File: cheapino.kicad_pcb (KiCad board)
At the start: 2 copper layers, 130.3 x 94.5 mm, 42 parts, among them K1 SW_Push, K10 SW_Push, K11 SW_Push, K12 SW_Push, K13 SW_Push, K14 SW_Push, K15 SW_Push, K16 SW_Push, K17 SW_Push, K18 SW_Push, K2 SW_Push, K3 SW_Push, K4 SW_Push, K5 SW_Push, K6 SW_Push, K7 SW_Push, K8 SW_Push, K9 SW_Push, U1 RP2040-Zero

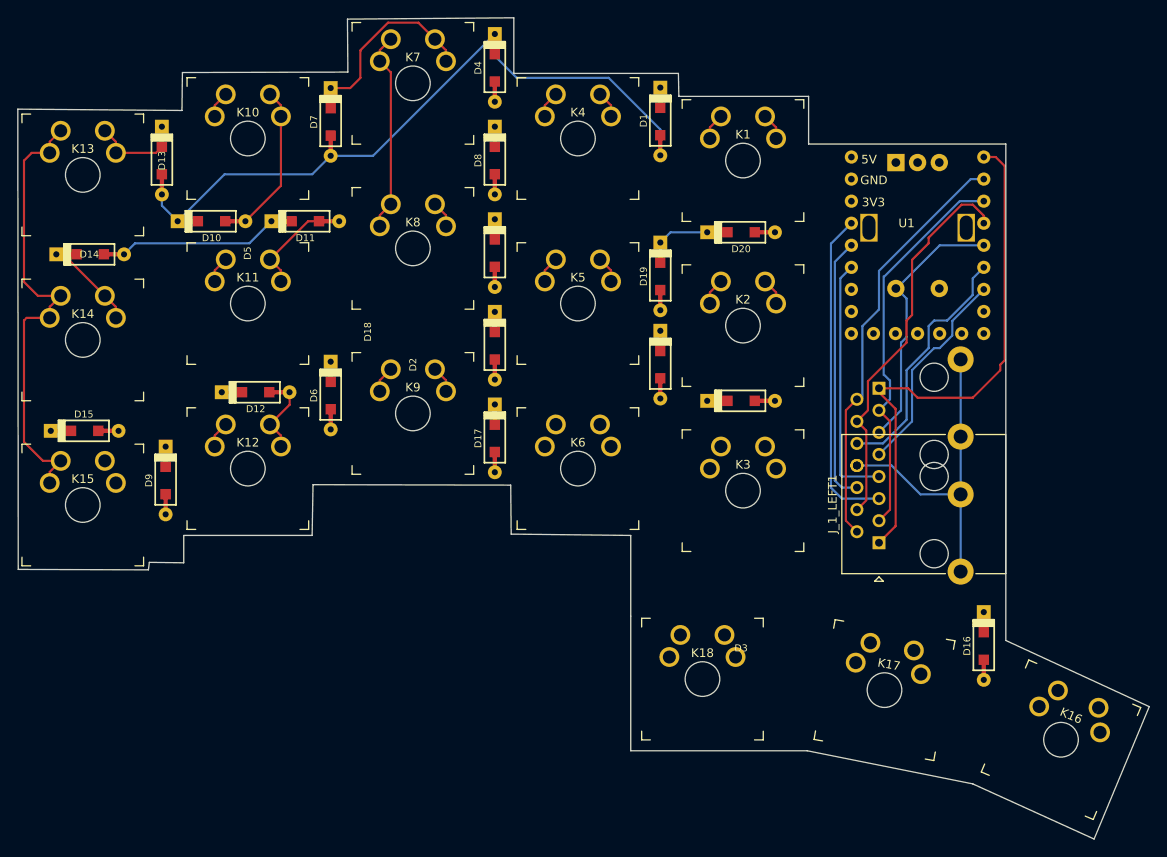
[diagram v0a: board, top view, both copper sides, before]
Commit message: passes drc
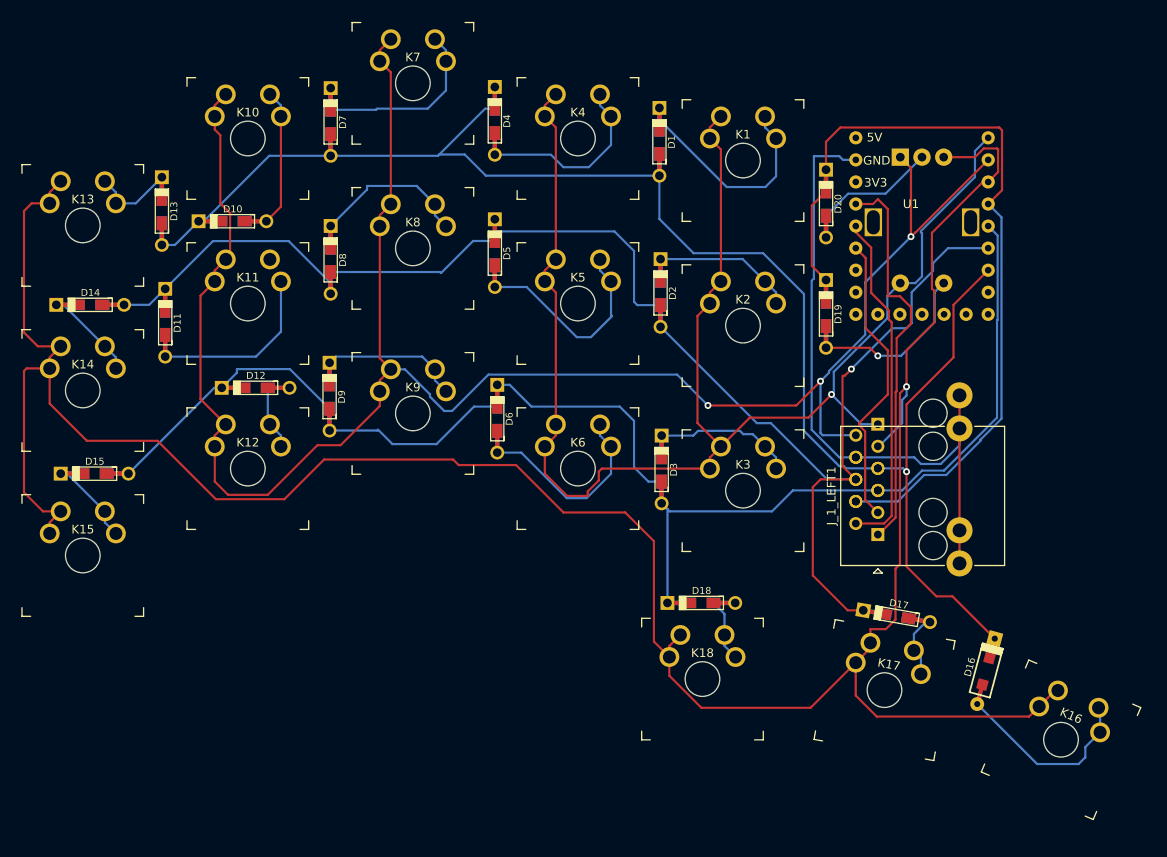
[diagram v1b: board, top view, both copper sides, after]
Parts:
- D1, D10, D11, D12, D13, D14, D15, D17, D18, D19, D2, D20, D3, D4, D5, D6, D7, D8, D9: footprint keyboard_parts:D_SOD123_axial -> keebio:Diode-dual
- moved D17 50.6 mm to (162.7, 115.3), turned to 170 degrees
- moved D18 38.0 mm to (140.2, 113.8), turned to 180 degrees
- moved D8 22.1 mm to (97.5, 74.3), turned to 90 degrees
- moved D9 21.2 mm to (97.4, 90.0), turned to 90 degrees
- moved D11 19.9 mm to (78.5, 81.5), turned to 90 degrees
- moved D19 19.6 mm to (154.6, 80.5), turned to 90 degrees
- moved D6 19.4 mm to (116.7, 92.6), turned to 90 degrees
- moved D3 12.1 mm to (135.6, 98.4), turned to 90 degrees
- moved D20 10.3 mm to (154.6, 67.8), turned to 90 degrees
- moved D2 8.26 mm to (135.5, 78.1), turned to 90 degrees
- moved D4 6.10 mm to (116.4, 58.3), turned to 90 degrees
- moved D13 5.82 mm to (78.1, 68.7), turned to 90 degrees
- moved D14 5.81 mm to (69.8, 79.5), turned to 180 degrees
- moved K13 5.81 mm to (69.0, 70.3)
- moved K14 5.81 mm to (69.0, 89.3)
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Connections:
- J_1_LEFT1 pad 1: ROW_1 -> REMOTE_COL_1
- J_1_LEFT1 pad 2: ROW_2 -> REMOTE_COL_2
- J_1_LEFT1 pad 3: ROW_3 -> REMOTE_COL_3
- J_1_LEFT1 pad 5: REMOTE_COL_1 -> ROW_3
- J_1_LEFT1 pad 6: REMOTE_COL_2 -> ROW_2
- J_1_LEFT1 pad 7: REMOTE_COL_3 -> ROW_1
- J_2_RIGHT1 pad 1: ROW_1 -> COL_1
- J_2_RIGHT1 pad 2: ROW_2 -> COL_2
- J_2_RIGHT1 pad 3: ROW_3 -> COL_3
- J_2_RIGHT1 pad 4: ROW_4 -> GND
- J_2_RIGHT1 pad 5: COL_1 -> ROW_1
- J_2_RIGHT1 pad 6: COL_2 -> ROW_2
- J_2_RIGHT1 pad 7: COL_3 -> ROW_3
- J_2_RIGHT1 pad 8: GND -> ROW_4
- U1 pad 0: ROW_1 -> COL_1
- U1 pad 1: ROW_2 -> COL_2
- U1 pad 2: ROW_3 -> COL_3
- U1 pad 4: COL_1 -> ROW_3
- U1 pad 5: COL_2 -> ROW_2
- U1 pad 6: COL_3 -> ROW_1
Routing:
- net COL_3: track 77.9 -> 293.8 mm, vias 0 -> 1
- net COL_2: track 64.3 -> 227.0 mm, vias 0 -> 3
- net COL_1: track 42.7 -> 173.0 mm, vias 0 -> 1
- net ROW_3: track 45.0 -> 156.5 mm
- net ROW_2: track 66.7 -> 167.2 mm, vias 0 -> 1
- net ROW_4: track 50.8 -> 91.1 mm
- net GND: track 37.7 -> 77.4 mm
- net ROW_1: track 139.0 -> 177.5 mm, vias 0 -> 1
- net Net-(D1-Pad1): track 3.07 -> 25.9 mm
- net Net-(D6-Pad2): track 0.00 -> 22.6 mm
- net Net-(D16-Pad2): track 0.00 -> 22.1 mm
- net Net-(D5-Pad2): track 3.07 -> 24.0 mm
- net Net-(D19-Pad2): track 0.00 -> 19.4 mm, vias 0 -> 1
- net Net-(D4-Pad2): track 3.07 -> 21.4 mm
- net Net-(D3-Pad1): track 0.00 -> 15.9 mm
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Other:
- board outline removed

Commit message: Rev 1, ordered from jlcpcb
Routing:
- net Net-(D11-Pad2): track 20.3 -> 23.4 mm
- added copper zone on B.Cu, net GND
- added copper zone on F.Cu, net GND
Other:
- board outline added: 139 x 102.6 mm
- board text added: "Cheapino"
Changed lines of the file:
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@@
   )
   (setup
+    (stackup
+      (layer "F.SilkS" (type "Top Silk Screen") (color "White"))
+      (layer "F.Paste" (type "Top Solder Paste"))
+      (layer "F.Mask" (type "Top Solder Mask") (color "Black") (thickness 0.01))
+      (layer "F.Cu" (type "copper") (thickness 0.035))
+      (layer "dielectric 1" (type "core") (thickness 1.51) (material "FR4") (epsilon_r 4.5) (loss_tangent 0.02))
+      (layer "B.Cu" (type "copper") (thickness 0.035))
+      (layer "B.Mask" (type "Bottom Solder Mask") (color "Black") (thickness 0.01))
+      (layer "B.Paste" (type "Bottom Solder Paste"))
+      (layer "B.SilkS" (type "Bottom Silk Screen") (color "White"))
+      (copper_finish "None")
+      (dielectric_constraints no)
+    )
     (pad_to_mask_clearance 0)
     (pcbplotparams
@@
     )
   )
+  (gr_line (start 76.2 52.705) (end 76.168088 53.943088) (layer "Edge.Cuts") (width 0.1))
+  (gr_arc (start 132.715001 134.619999) (mid 129.686086 133.203914) (end 128.270001 130.174999) (layer "Edge.Cuts") (width 0.1))
+  (gr_line (start 95.25 110.49) (end 84.455008 110.49) (layer "Edge.Cuts") (width 0.1))
+  (gr_line (start 125.462462 111.125) (end 118.745001 111.124999) (layer "Edge.Cuts") (width 0.1))
+  (gr_arc (start 76.2 52.705) (mid 77.50191 49.56191) (end 80.645 48.26) (layer "Edge.Cuts") (width 0.1))
+  (gr_line (start 118.11 43.815) (end 118.125468 45.72) (layer "Edge.Cuts") (width 0.1))
+  (gr_arc (start 193.04 120.65) (mid 195.786896 123.226503) (end 195.58 127) (layer "Edge.Cuts") (width 0.1))
+  (gr_line (start 98.425 41.275) (end 115.920532 41.275) (layer "Edge.Cuts") (width 0.1))
+  (gr_arc (start 185.42 117.475) (mid 181.747396 115.423368) (end 179.736912 111.728088) (layer "Edge.Cuts") (width 0.1))
+  (gr_arc (start 95.885 43.815) (mid 96.597006 41.987006) (end 98.425 41.275) (layer "Edge.Cuts") (width 0.1))
+  (gr_arc (start 99.695 106.68) (mid 98.177205 109.407156) (end 95.25 110.49) (layer "Edge.Cuts") (width 0.1))
+  (gr_arc (start 76.168088 53.943088) (mid 74.866178 57.086178) (end 71.723088 58.388088) (layer "Edge.Cuts") (width 0.1))
+  (gr_line (start 179.704999 61.595001) (end 179.736912 111.728088) (layer "Edge.Cuts") (width 0.1))
+  (gr_line (start 76.80309 120.04691) (end 61.595 120.015) (layer "Edge.Cuts") (width 0.1))
+  (gr_line (start 95.885 43.815) (end 95.885 45.512538) (layer "Edge.Cuts") (width 0.1))
+  (gr_line (start 185.42 117.475) (end 193.04 120.65) (layer "Edge.Cuts") (width 0.1))
+  (gr_arc (start 57.15 62.865) (mid 58.45191 59.72191) (end 61.595 58.42) (layer "Edge.Cuts") (width 0.1))
+  (gr_line (start 57.15 115.57) (end 57.15 62.865) (layer "Edge.Cuts") (width 0.1))
+  (gr_arc (start 175.259999 57.150001) (mid 178.403089 58.451911) (end 179.704999 61.595001) (layer "Edge.Cuts") (width 0.1))
+  (gr_arc (start 158.75 57.15) (mid 157.39304 56.60196) (end 156.845 55.245) (layer "Edge.Cuts") (width 0.1))
+  (gr_line (start 80.645 48.26) (end 93.137538 48.26) (layer "Edge.Cuts") (width 0.1))
+  (gr_line (start 136.525 50.8) (end 152.4 50.8) (layer "Edge.Cuts") (width 0.1))
+  (gr_arc (start 61.595 120.015) (mid 58.45191 118.71309) (end 57.15 115.57) (layer "Edge.Cuts") (width 0.1))
+  (gr_arc (start 118.745001 111.124999) (mid 115.586582 109.825689) (end 114.25675 106.68) (layer "Edge.Cuts") (width 0.1))
+  (gr_line (start 81.248097 114.3) (end 81.24809 115.60191) (layer "Edge.Cuts") (width 0.1))
+  (gr_arc (start 115.920532 41.275) (mid 117.52596 42.104784) (end 118.11 43.815) (layer "Edge.Cuts") (width 0.1))
+  (gr_line (start 195.58 127) (end 189.477795 140.97) (layer "Edge.Cuts") (width 0.1))
+  (gr_arc (start 81.24809 115.60191) (mid 79.94618 118.745) (end 76.80309 120.04691) (layer "Edge.Cuts") (width 0.1))
+  (gr_line (start 120.87293 48.26) (end 133.35 48.26) (layer "Edge.Cuts") (width 0.1))
+  (gr_arc (start 81.248097 114.3) (mid 82.162819 111.798826) (end 84.455008 110.49) (layer "Edge.Cuts") (width 0.1))
+  (gr_line (start 61.595 58.42) (end 71.723088 58.388088) (layer "Edge.Cuts") (width 0.1))
+  (gr_arc (start 189.477795 140.97) (mid 187.028194 143.488423) (end 183.515 143.51) (layer "Edge.Cuts") (width 0.1))
+  (gr_arc (start 152.4 50.8) (mid 155.54309 52.10191) (end 156.845 55.245) (layer "Edge.Cuts") (width 0.1))
+  (gr_arc (start 95.885 45.512538) (mid 95.051621 47.426621) (end 93.137538 48.26) (layer "Edge.Cuts") (width 0.1))
+  (gr_arc (start 120.87293 48.26) (mid 118.970668 47.5617) (end 118.125468 45.72) (layer "Edge.Cuts") (width 0.1))
+  (gr_arc (start 133.35 48.26) (mid 134.589877 48.708896) (end 135.255002 49.847496) (layer "Edge.Cuts") (width 0.1))
+  (gr_arc (start 125.462462 111.125) (mid 127.617173 111.899097) (end 128.669372 113.932538) (layer "Edge.Cuts") (width 0.1))
+  (gr_line (start 128.669372 113.932538) (end 128.270001 130.174999) (layer "Edge.Cuts") (width 0.1))
+  (gr_line (start 111.04984 103.47309) (end 103.47309 103.47309) (layer "Edge.Cuts") (width 0.1))
+  (gr_arc (start 111.04984 103.47309) (mid 113.401953 104.327887) (end 114.25675 106.68) (layer "Edge.Cuts") (width 0.1))
+  (gr_line (start 158.75 57.15) (end 175.259999 57.150001) (layer "Edge.Cuts") (width 0.1))
+  (gr_arc (start 99.695 106.68) (mid 100.887993 104.256516) (end 103.47309 103.47309) (layer "Edge.Cuts") (width 0.1))
+  (gr_arc (start 136.525 50.8) (mid 135.760115 50.496928) (end 135.255002 49.847496) (layer "Edge.Cuts") (width 0.1))
+  (gr_arc (start 132.715001 134.619999) (mid 158.726548 135.57044) (end 183.515 143.51) (layer "Edge.Cuts") (width 0.1))
+  (gr_text "Cheapino" (at 168.91 85.09) (layer "B.SilkS")
+    (effects (font (size 2 2) (thickness 0.15)) (justify mirror))
+  )
   (gr_text "3V3" (at 160.274 65.405) (layer "F.SilkS")
     (effects (font (size 1 1) (thickness 0.15)))
   )
+  (gr_text "Cheapino" (at 168.91 85.09) (layer "F.SilkS")
+    (effects (font (size 2 2) (thickness 0.15)))
+  )
   (gr_text "GND" (at 160.401 62.865) (layer "F.SilkS")
     (effects (font (size 1 1) (thickness 0.15)))
@@
   (segment (start 91.81 56.515) (end 91.81 57.785) (width 0.25) (layer "B.Cu") (net 13))
   (segment (start 90.54 55.245) (end 91.81 56.515) (width 0.25) (layer "B.Cu") (net 13))
+  (segment (start 90.54 74.245) (end 91.81 75.515) (width 0.25) (layer "B.Cu") (net 14))
   (segment (start 88.937 85.434) (end 91.81 82.561) (width 0.25) (layer "B.Cu") (net 14))
   (segment (start 91.81 82.561) (end 91.81 76.785) (width 0.25) (layer "B.Cu") (net 14))
   (segment (start 78.486 85.434) (end 88.937 85.434) (width 0.25) (layer "B.Cu") (net 14))
+  (segment (start 91.81 75.515) (end 91.81 76.785) (width 0.25) (layer "B.Cu") (net 14))
   (segment (start 91.81 94.515) (end 91.81 95.785) (width 0.25) (layer "B.Cu") (net 15))
   (segment (start 90.3 89.027) (end 90.3 93.005) (width 0.25) (layer "B.Cu") (net 15))
@@
   (segment (start 161.671 84.709) (end 159.131 82.169) (width 0.25) (layer "F.Cu") (net 31))
   (segment (start 161.671 89.789) (end 161.671 84.709) (width 0.25) (layer "F.Cu") (net 31))
+  (zone (net 27) (net_name "GND") (layer "F.Cu") (hatch edge 0.508)
+    (connect_pads (clearance 0.508))
+    (min_thickness 0.254) (filled_areas_thickness no)
+    (fill yes (thermal_gap 0.508) (thermal_bridge_width 0.508))
+    (polygon
+      (pts
+        (xy 201.93 160.655)
+        (xy 38.1 146.05)
+        (xy 41.91 34.925)
+        (xy 221.615 34.925)
+      )
+    )
+  )
+  (zone (net 27) (net_name "GND") (layer "B.Cu") (hatch edge 0.508)
+    (connect_pads (clearance 0.508))
+    (min_thickness 0.254) (filled_areas_thickness no)
+    (fill yes (thermal_gap 0.508) (thermal_bridge_width 0.508))
+    (polygon
+      (pts
+        (xy 225.425 36.195)
+        (xy 201.295 165.1)
+        (xy 37.465 147.32)
+        (xy 43.18 34.925)
+      )
+    )
+  )
 )

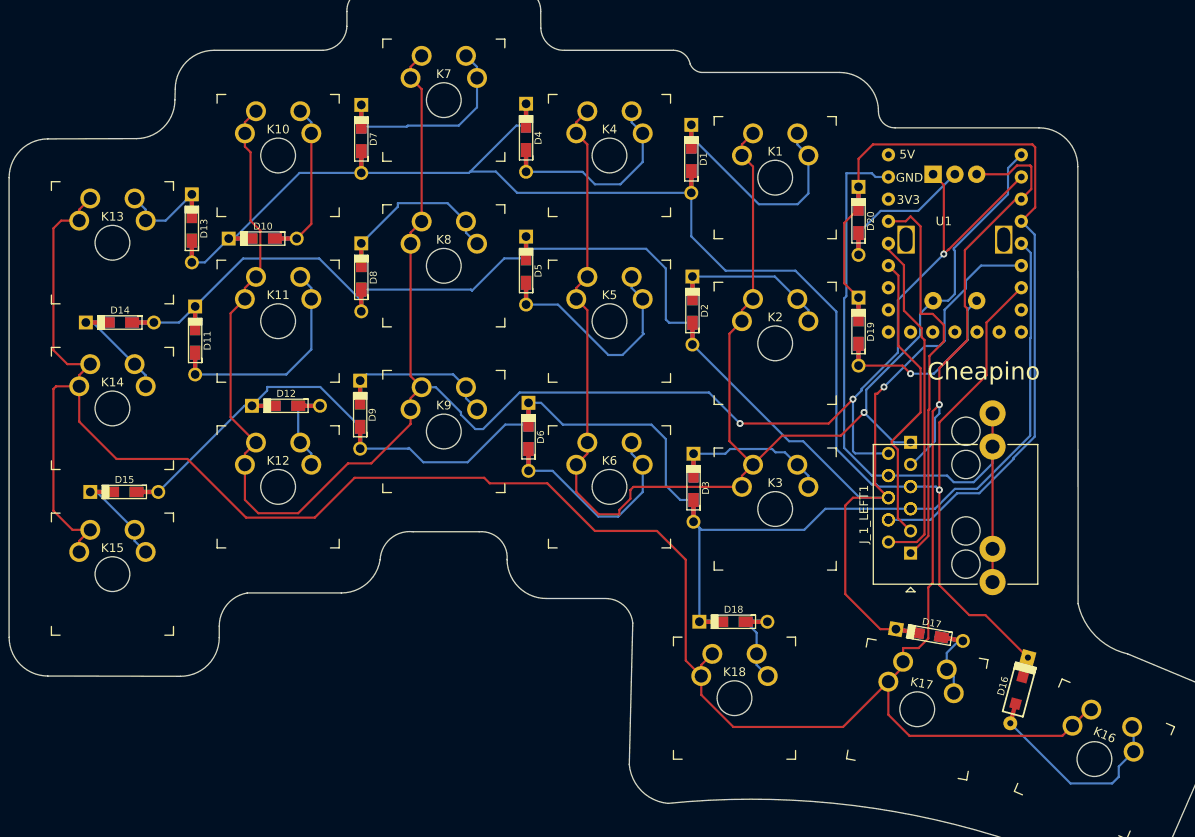
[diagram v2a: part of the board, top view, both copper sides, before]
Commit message: 1.1: Rounded tracks and teardrops
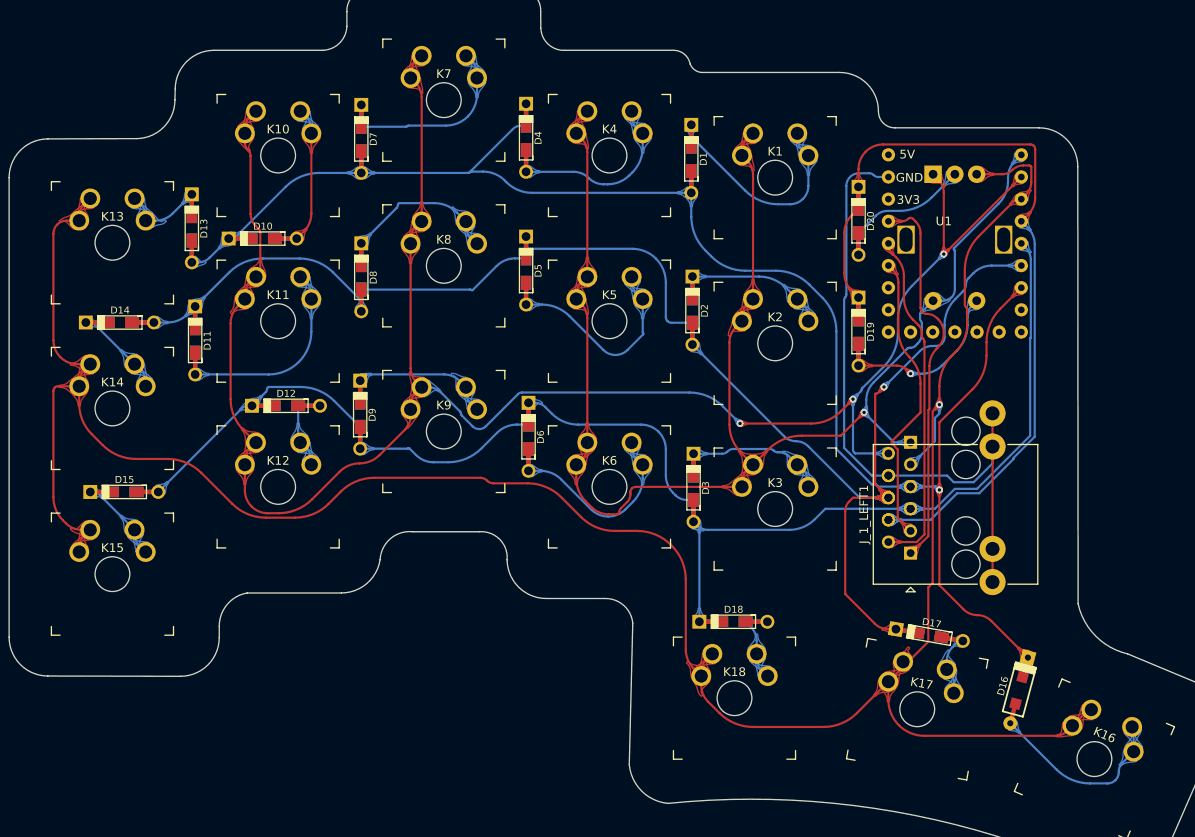
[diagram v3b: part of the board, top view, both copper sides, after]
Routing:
- net COL_3: track 293.8 -> 288.1 mm
- net COL_2: track 227.0 -> 222.7 mm
- net ROW_1: track 177.5 -> 175.0 mm
- net ROW_2: track 167.2 -> 164.8 mm
- net ROW_3: track 156.5 -> 154.3 mm
- net COL_1: track 173.0 -> 171.8 mm
- net REMOTE_COL_1: track 45.4 -> 44.3 mm
- net ROW_4: track 91.1 -> 90.3 mm
- net GND: track 77.4 -> 76.6 mm
- net Net-(D1-Pad1): track 25.9 -> 25.2 mm
- net Net-(D6-Pad2): track 22.6 -> 22.0 mm
- net Net-(D4-Pad2): track 21.4 -> 20.7 mm
- net Net-(D11-Pad2): track 23.4 -> 22.8 mm
- net Net-(D5-Pad2): track 24.0 -> 23.5 mm
- net Net-(D19-Pad2): track 19.4 -> 18.9 mm
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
